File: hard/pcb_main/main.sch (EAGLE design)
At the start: 154 parts

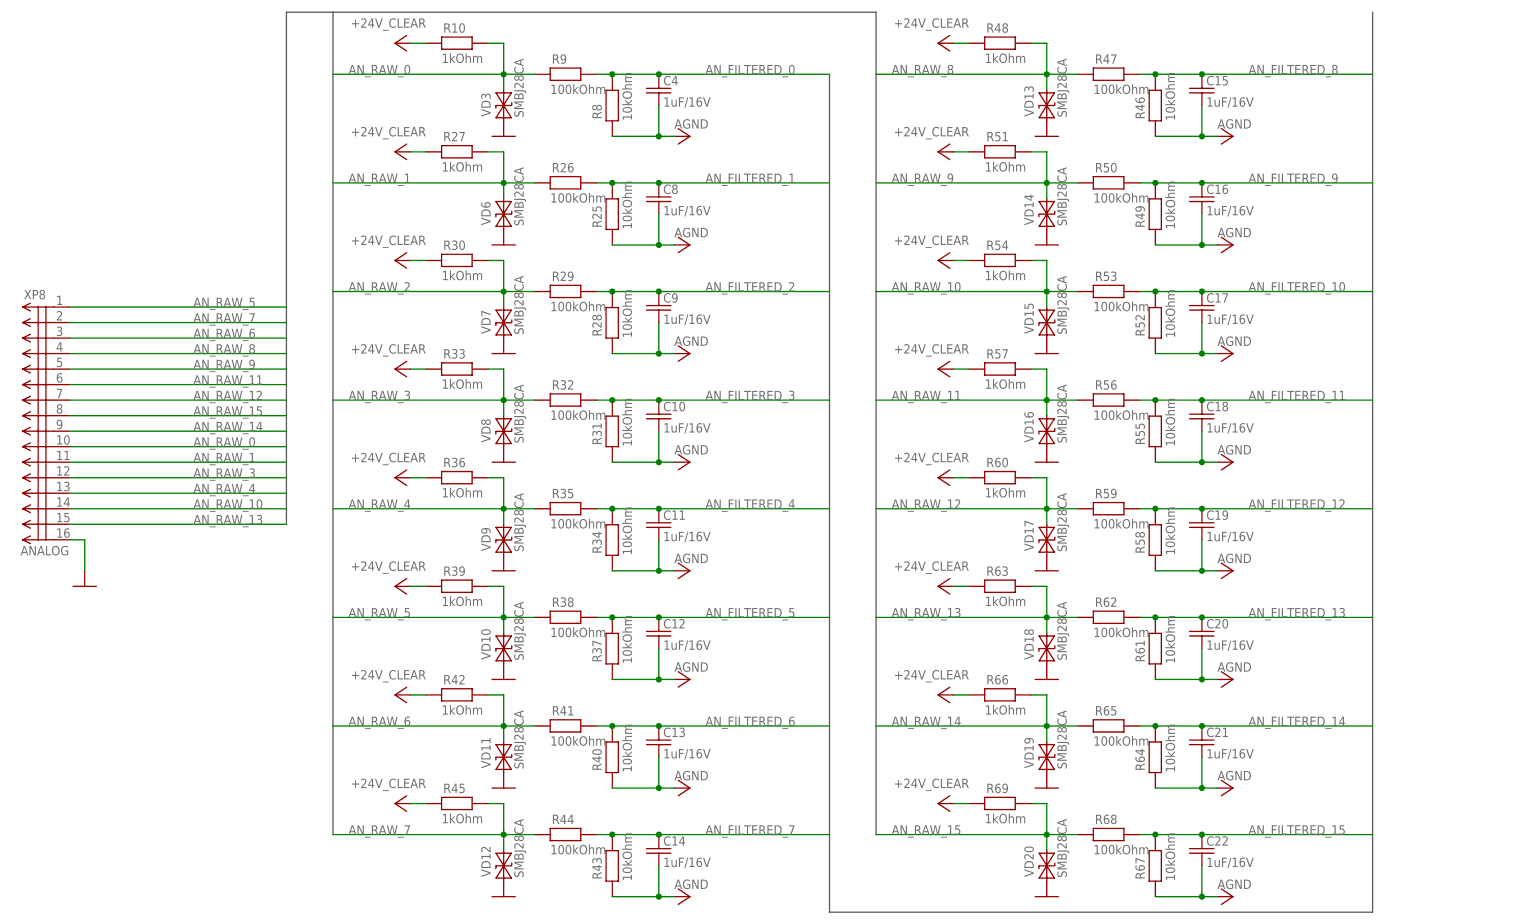
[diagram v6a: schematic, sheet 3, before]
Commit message: analog inputs fixed and rerouted
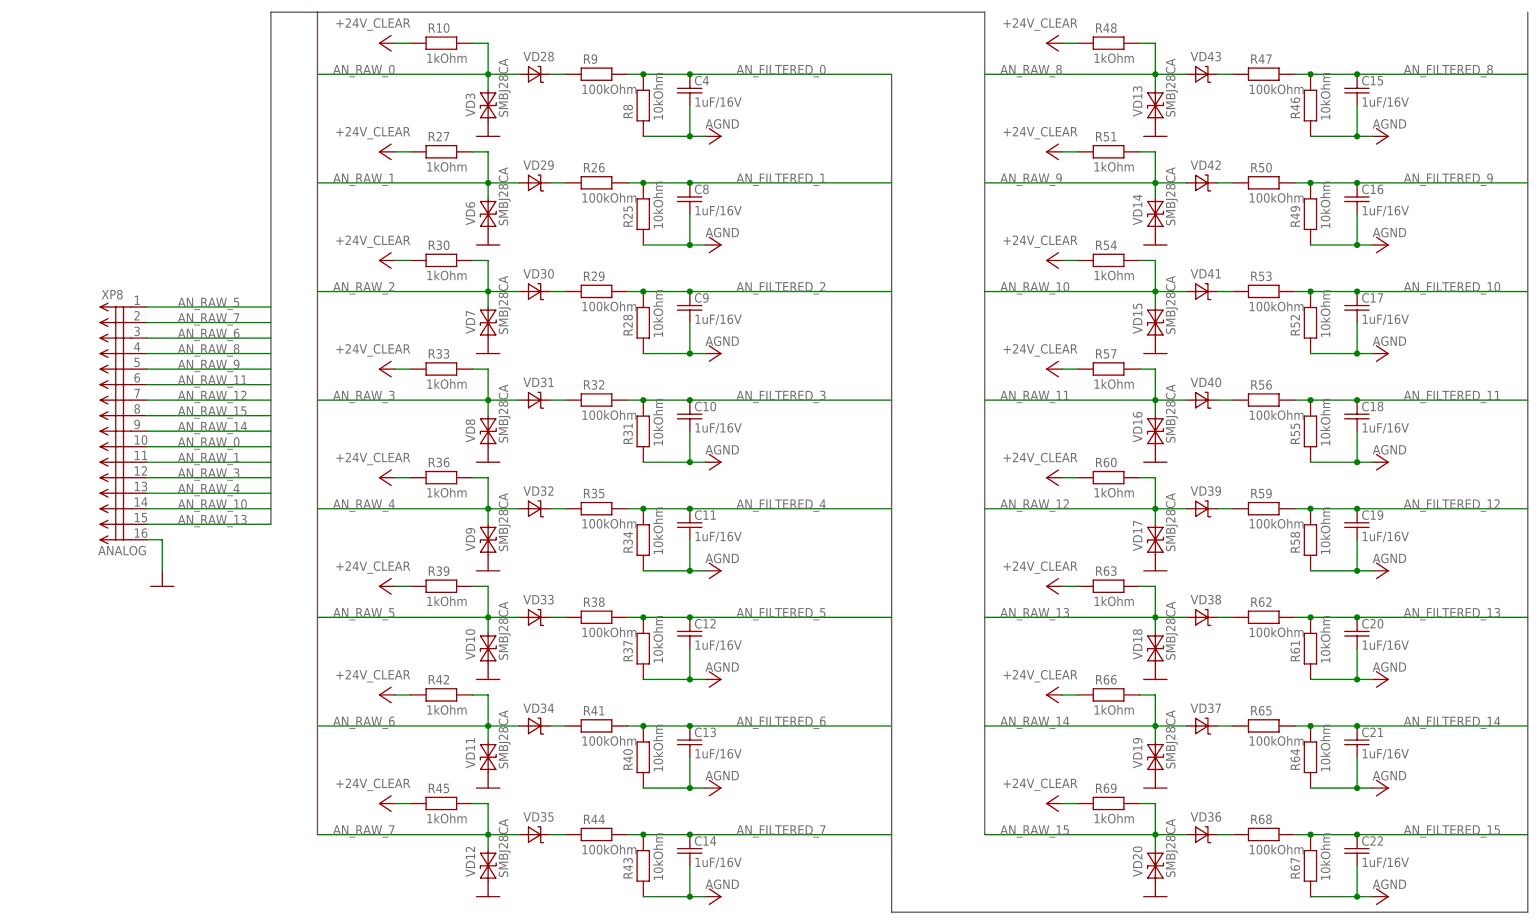
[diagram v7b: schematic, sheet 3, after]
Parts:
- removed DA3: BTS6143D, transistor-fet:BTS6143D
- added D2, D3, D4, D5: AUIPS7125R, transistor-fet:AUIPS7125R
- added R1: 1kOhm, rcl:R-EU_R0805
- added VD28, VD29, VD30, VD31, VD32, VD33, VD34, VD35, VD36, VD37, VD38, VD39, VD40, VD41, VD42, VD43: (no value), diode:DIODE-SCHOTTKY-SOD323
- R5, R6: value 3.3kOhm -> 1kOhm; PARTNO ERJ6GEYJ332V -> ERJ6GEYJ102V
- VD21: value 1000V/3A -> 600V/6A; device diode:DIODE-STANDARD-SMC -> diode:IDD06SG60C; PARTNO RS3M -> IDD06SG60C
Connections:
- new net N$30: R9.1, VD28.C
- new net N$31: R26.1, VD29.C
- new net N$32: R44.1, VD35.C
- new net N$33: R41.1, VD34.C
- new net N$34: R38.1, VD33.C
- new net N$35: R35.1, VD32.C
- new net N$36: R32.1, VD31.C
- new net N$37: R29.1, VD30.C
- new net N$38: R47.1, VD43.C
- new net N$39: R53.1, VD41.C
- new net N$40: R50.1, VD42.C
- new net N$41: R56.1, VD40.C
- new net N$42: R59.1, VD39.C
- new net N$43: R65.1, VD37.C
- new net N$44: R62.1, VD38.C
- new net N$45: R68.1, VD36.C
- net AN_RAW_0: now also VD28.A; no longer R9.1
- net AN_RAW_1: now also VD29.A; no longer R26.1
- net AN_RAW_10: now also VD41.A; no longer R53.1
- net AN_RAW_11: now also VD40.A; no longer R56.1
- net AN_RAW_12: now also VD39.A; no longer R59.1
- net AN_RAW_13: now also VD38.A; no longer R62.1
- net AN_RAW_14: now also VD37.A; no longer R65.1
- net AN_RAW_15: now also VD36.A; no longer R68.1
- net AN_RAW_2: now also VD30.A; no longer R29.1
- net AN_RAW_3: now also VD31.A; no longer R32.1
- net AN_RAW_4: now also VD32.A; no longer R35.1
- net AN_RAW_5: now also VD33.A; no longer R38.1
- net AN_RAW_6: now also VD34.A; no longer R41.1
- net AN_RAW_7: now also VD35.A; no longer R44.1
- net AN_RAW_8: now also VD43.A; no longer R47.1
- net AN_RAW_9: now also VD42.A; no longer R50.1
- net N$1: now also D1.1.TC, D2.IN; no longer DA3.IN, R6.1
- net N$10: now also D2.IFB, R7.2; no longer D1.3.TE, D1.4.DC
- net N$11: now also D1.2.TE, D1.3.TE, D1.4.TE, R1.1, R5.1, R6.1, R7.1; no longer D1.2.DC
- net N$3: now also D1.2.TC, D3.IN; no longer D1.1.TC, R7.2
- net N$4: now also D1.3.TC, D4.IN; no longer D1.2.TC, R5.2
- net N$5: now also D1.4.TC, D5.IN; no longer R6.2, R7.1
- net N$6: now also D5.IFB, R6.2; no longer D1.3.TC, DA3.IS
- net N$8: now also D4.IFB, R5.2; no longer D1.3.DA, R5.1
- net N$9: now also D3.IFB, R1.2; no longer D1.2.TE, D1.3.DC
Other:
- moved on the sheet: C10, C11, C12, C13, C14, C15, C16, C17, C18, C19, C20, C21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

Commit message: nop
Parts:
- added D10, D7, D8, D9: AUIPS7125R, transistor-fet:AUIPS7125R
- added D6: TCMT4100, optocoupler:TCMT4100
- added R72, R73, R74, R75: 1kOhm, rcl:R-EU_R0805
- D1: PARTNO * -> TCMT4100
- VD10, VD11, VD12, VD13, VD15, VD16, VD17, VD18, VD19, VD20, VD23, VD24, VD25, VD27, VD3, VD6, VD7, VD8, VD9: value SMBJ28CA -> SMBJ24CA; PARTNO SMBJ28CA-TR -> SMBJ24CA
- VD14: value SMBJ28CA -> SMBJ24CA; PARTNO SMBJ30CA -> SMBJ24CA
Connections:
- removed net N$11: D1.1.TE, D1.2.TE, D1.3.TE, D1.4.TE, R1.1, R5.1, R6.1, R7.1
- new net N$46: D6.1.TC, D7.IN
- new net N$47: D6.2.TC, D8.IN
- new net N$48: D6.3.TC, D9.IN
- new net N$49: D10.IN, D6.4.TC
- new net N$50: D10.IFB, R75.2
- new net N$51: D9.IFB, R74.2
- new net N$52: D8.IFB, R73.2
- new net N$53: D7.IFB, R72.2
- net GND: now also D1.1.TE, D1.2.TE, D1.3.TE, D1.4.TE, D6.1.TE, D6.2.TE, D6.3.TE, D6.4.TE, R1.1, R5.1, R6.1, R7.1, R72.1, R73.1, R74.1, R75.1
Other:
- moved on the sheet: D1.1, D1.2, D1.3, D1.4, D2, D3, D4, D5, R1, R5, R6, R7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
